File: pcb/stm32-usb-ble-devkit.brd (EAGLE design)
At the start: 90 x 50 mm, 91 parts, among them CN1 USB-MICROB-2TABS, CN2 USB-C-2.0-FEMALE, CN3 USB-C-2.0-FEMALE, Q2 AO3402, Q4 AO3401, Q6 AO3401, Q8 AO3401, U1 STM32F103-48LQFP, U2 STM32F205-64, U3 TUSB320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

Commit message: pcb: Fix symbol orientation and add PSU caps
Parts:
- added C20, C21: 100n, tuetuopay:0805
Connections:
- net +3V3: now also C21.1
- net +5V: now also C20.1
- net GND: now also C20.2, C21.2
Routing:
- net +5V: track 62.0 -> 59.5 mm
- net +3V3: track 245.8 -> 244.8 mm, vias 14 -> 13
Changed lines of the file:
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@@
 <?xml version="1.0" encoding="utf-8"?>
 <!DOCTYPE eagle SYSTEM "eagle.dtd">
-<eagle version="9.0.0">
+<eagle version="9.1.3">
 <drawing>
 <settings>
@@
 <param name="checkStop" value="0"/>
 <param name="checkValues" value="0"/>
+<param name="checkNames" value="1"/>
+<param name="checkWireStubs" value="1"/>
+<param name="checkPolygonWidth" value="0"/>
 <param name="useDiameter" value="13"/>
 <param name="maxErrors" value="50"/>
@@
 <attribute name="VALUE" x="51.265" y="26.238" size="0.0254" layer="27"/>
 </element>
+<element name="C20" library="tuetuopay" package="0805" value="100n" x="-9.9" y="-9.3"/>
+<element name="C21" library="tuetuopay" package="0805" value="100n" x="-9.9" y="-15.45"/>
 </elements>
 <signals>
@@
 <contactref element="C15" pad="2"/>
 <contactref element="C16" pad="2"/>
-<contactref element="C18" pad="1"/>
-<contactref element="U6" pad="2"/>
 <wire x1="12.15" y1="14.75" x2="13.425" y2="13.475" width="0.15" layer="1"/>
 <wire x1="13.425" y1="13.475" x2="14.2432" y2="13.475" width="0.15" layer="1"/>
@@
 <wire x1="16.7" y1="33" x2="13.69644375" y2="33" width="0.15" layer="1"/>
 <wire x1="13.35" y1="32.65355625" x2="13.35" y2="32.4" width="0.15" layer="1"/>
-<wire x1="22.65" y1="37" x2="24.5" y2="37" width="0.4" layer="1"/>
-<wire x1="24.5" y1="37" x2="24.55" y2="37.05" width="0.6" layer="1"/>
-<via x="22.65" y="37" extent="1-16" drill="0.3"/>
 <wire x1="22.65" y1="37" x2="20.7" y2="37" width="0.4" layer="16"/>
 <wire x1="20.7" y1="37" x2="19" y2="35.3" width="0.4" layer="16"/>
 <via x="16.7" y="33" extent="1-16" drill="0.3"/>
 <wire x1="19" y1="35.3" x2="16.7" y2="33" width="0.4" layer="16"/>
-<wire x1="24.55" y1="37.05" x2="25.5" y2="37.05" width="0.4" layer="1"/>
 <wire x1="28.05" y1="39.6" x2="31.05" y2="39.6" width="0.4" layer="1"/>
 <wire x1="31.05" y1="39.6" x2="32.85" y2="39.6" width="0.4" layer="1"/>
@@
 <wire x1="15.73" y1="38.57" x2="19" y2="35.3" width="0.4" layer="16"/>
 <wire x1="5.78649375" y1="38.57" x2="15.73" y2="38.57" width="0.4" layer="16"/>
+<contactref element="C18" pad="1"/>
+<contactref element="U6" pad="2"/>
+<contactref element="C21" pad="1"/>
+<wire x1="22.65" y1="37" x2="24.5" y2="37" width="0.4" layer="1"/>
+<wire x1="24.5" y1="37" x2="24.55" y2="37.05" width="0.6" layer="1"/>
+<wire x1="24.55" y1="37.05" x2="25.5" y2="37.05" width="0" layer="19" extent="1-1"/>
+<wire x1="22.65" y1="37" x2="22.65" y2="37" width="0" layer="19" extent="1-16"/>
+<wire x1="-10.85" y1="-15.45" x2="14.7" y2="9.45" width="0" layer="19" extent="1-1"/>
 </signal>
 <signal name="GND">
@@
 <vertex x="-6.9" y="33.75"/>
 </polygon>
-<wire x1="29.3" y1="22.48" x2="26.85" y2="26.43" width="0" layer="19" extent="1-1"/>
+<contactref element="C20" pad="2"/>
+<contactref element="C21" pad="2"/>
+<wire x1="68.5" y1="38.1" x2="74.65" y2="36.05" width="0" layer="19" extent="1-1"/>
+<wire x1="64.65" y1="34.05" x2="68.5" y2="38.1" width="0" layer="19" extent="1-1"/>
+<wire x1="52.75" y1="33.15" x2="64.65" y2="34.05" width="0" layer="19" extent="1-1"/>
+<wire x1="52.75" y1="29.25" x2="52.75" y2="33.15" width="0" layer="19" extent="1-1"/>
+<wire x1="45.43" y1="33.29" x2="52.75" y2="33.15" width="0" layer="19" extent="1-1"/>
+<wire x1="40.43" y1="35.29" x2="45.43" y2="33.29" width="0" layer="19" extent="1-1"/>
+<wire x1="37.55" y1="33" x2="40.43" y2="35.29" width="0" layer="19" extent="1-1"/>
+<wire x1="37.5375" y1="31.05" x2="37.55" y2="33" width="0" layer="19" extent="1-1"/>
+<wire x1="40.43" y1="39.29" x2="40.43" y2="35.29" width="0" layer="19" extent="1-1"/>
+<wire x1="42.43" y1="41.79" x2="40.43" y2="39.29" width="0" layer="19" extent="1-1"/>
+<wire x1="41.43" y1="45.885" x2="42.43" y2="41.79" width="0" layer="19" extent="1-1"/>
 <wire x1="41.58" y1="48.56" x2="41.43" y2="45.885" width="0" layer="19" extent="1-1"/>
-<wire x1="17.9" y1="17.48" x2="16.05" y2="14.75" width="0" layer="19" extent="1-1"/>
+<wire x1="43.88" y1="48.56" x2="41.58" y2="48.56" width="0" layer="19" extent="1-1"/>
+<wire x1="46.48" y1="48.56" x2="43.88" y2="48.56" width="0" layer="19" extent="1-1"/>
+<wire x1="38.98" y1="48.56" x2="41.58" y2="48.56" width="0" layer="19" extent="1-1"/>
+<wire x1="36.95" y1="42" x2="40.43" y2="39.29" width="0" layer="19" extent="1-1"/>
+<wire x1="34.8375" y1="45.9" x2="36.95" y2="42" width="0" layer="19" extent="1-1"/>
+<wire x1="48.93" y1="39.79" x2="42.43" y2="41.79" width="0" layer="19" extent="1-1"/>
+<wire x1="52.6" y1="40.95" x2="48.93" y2="39.79" width="0" layer="19" extent="1-1"/>
+<wire x1="56.7" y1="43.95" x2="52.6" y2="40.95" width="0" layer="19" extent="1-1"/>
+<wire x1="53.5125" y1="47.85" x2="56.7" y2="43.95" width="0" layer="19" extent="1-1"/>
+<wire x1="31.65" y1="25.9" x2="37.5375" y2="31.05" width="0" layer="19" extent="1-1"/>
+<wire x1="29.3" y1="22.48" x2="31.65" y2="25.9" width="0" layer="19" extent="1-1"/>
+<wire x1="26.85" y1="26.43" x2="29.3" y2="22.48" width="0" layer="19" extent="1-1"/>
+<wire x1="20.35" y1="26.43" x2="26.85" y2="26.43" width="0" layer="19" extent="1-1"/>
+<wire x1="16.7" y1="29.1" x2="20.35" y2="26.43" width="0" layer="19" extent="1-1"/>
 <wire x1="14.15" y1="32.4" x2="16.7" y2="29.1" width="0" layer="19" extent="1-1"/>
-<wire x1="30.85" y1="13.2" x2="26.85" y2="15.03" width="0" layer="19" extent="1-1"/>
-<wire x1="52.6" y1="40.95" x2="56.7" y2="43.95" width="0" layer="19" extent="1-1"/>
+<wire x1="13.75" y1="32.4" x2="14.15" y2="32.4" width="0" layer="19" extent="1-1"/>
+<wire x1="18.4" y1="33" x2="16.7" y2="29.1" width="0" layer="19" extent="1-1"/>
+<wire x1="20.7" y1="36.65" x2="18.4" y2="33" width="0" layer="19" extent="1-1"/>
+<wire x1="22.65" y1="38.9" x2="20.7" y2="36.65" width="0" layer="19" extent="1-1"/>
+<wire x1="24.55" y1="39.35" x2="22.65" y2="38.9" width="0" layer="19" extent="1-1"/>
+<wire x1="9.9375" y1="37.65" x2="13.75" y2="32.4" width="0" layer="19" extent="1-1"/>
+<wire x1="7.355" y1="36.5" x2="9.9375" y2="37.65" width="0" layer="19" extent="1-1"/>
+<wire x1="2.6" y1="21.42" x2="2.6" y2="28.98" width="0" layer="19" extent="1-1"/>
 <wire x1="11.55" y1="10.8375" x2="6.78" y2="12.78" width="0" layer="19" extent="1-1"/>
 <wire x1="15.1" y1="9.45" x2="11.55" y2="10.8375" width="0" layer="19" extent="1-1"/>
+<wire x1="15.5" y1="9.45" x2="15.1" y2="9.45" width="0" layer="19" extent="1-1"/>
+<wire x1="16.05" y1="14.75" x2="15.5" y2="9.45" width="0" layer="19" extent="1-1"/>
+<wire x1="17.9" y1="17.48" x2="16.05" y2="14.75" width="0" layer="19" extent="1-1"/>
+<wire x1="12.15" y1="16.45" x2="16.05" y2="14.75" width="0" layer="19" extent="1-1"/>
+<wire x1="26.85" y1="15.03" x2="29.3" y2="22.48" width="0" layer="19" extent="1-1"/>
+<wire x1="30.85" y1="13.2" x2="26.85" y2="15.03" width="0" layer="19" extent="1-1"/>
+<wire x1="25.05" y1="9.9375" x2="26.85" y2="15.03" width="0" layer="19" extent="1-1"/>
+<wire x1="36.45" y1="6.95" x2="30.85" y2="13.2" width="0" layer="19" extent="1-1"/>
+<wire x1="43.6" y1="24" x2="37.5375" y2="31.05" width="0" layer="19" extent="1-1"/>
+<wire x1="45.05" y1="24" x2="43.6" y2="24" width="0" layer="19" extent="1-1"/>
+<wire x1="39.45" y1="19.85" x2="43.6" y2="24" width="0" layer="19" extent="1-1"/>
+<wire x1="39.45" y1="18.4" x2="39.45" y2="19.85" width="0" layer="19" extent="1-1"/>
+<wire x1="-8.95" y1="-9.3" x2="2.6" y2="12.78" width="0" layer="19" extent="1-1"/>
+<wire x1="-8.95" y1="-15.45" x2="-8.95" y2="-9.3" width="0" layer="19" extent="1-1"/>
 </signal>
 <signal name="STLINK_PC13">
@@
 <contactref element="Q6" pad="2"/>
 <contactref element="Q8" pad="2"/>
-<contactref element="C19" pad="1"/>
-<contactref element="U6" pad="3"/>
 <contactref element="D1" pad="3"/>
 <contactref element="Q4" pad="3"/>
@@
 <wire x1="15.45" y1="43.5556625" x2="15.45" y2="39" width="0.4" layer="1"/>
 <wire x1="15.45" y1="39" x2="14.9" y2="38.45" width="0.4" layer="1"/>
-<wire x1="20.7" y1="34.75" x2="24.55" y2="34.75" width="0.4" layer="1"/>
 <via x="14.9" y="36.65" extent="1-16" drill="0.3"/>
 <wire x1="14.9" y1="36.65" x2="16.3" y2="36.65" width="0.4" layer="16"/>
@@
 <via x="17.55" y="35.4" extent="1-16" drill="0.3"/>
 <wire x1="17.55" y1="35.4" x2="18.2" y2="34.75" width="0.4" layer="1"/>
-<wire x1="18.2" y1="34.75" x2="20.7" y2="34.75" width="0.4" layer="1"/>
 <via x="16.4" y="12.95" extent="1-16" drill="0.4"/>
 <wire x1="16.4" y1="12.95" x2="15.25" y2="14.1" width="0.4" layer="16"/>
@@
 <wire x1="20.675" y1="17.668625" x2="20.675" y2="24.325" width="0.4" layer="16"/>
 <wire x1="15.9" y1="29.1" x2="15.9" y2="33.75" width="0.4" layer="16"/>
+<contactref element="C19" pad="1"/>
+<contactref element="U6" pad="3"/>
+<contactref element="C20" pad="1"/>
+<wire x1="20.7" y1="34.75" x2="24.55" y2="34.75" width="0.4" layer="1"/>
+<wire x1="18.2" y1="34.75" x2="20.7" y2="34.75" width="0" layer="19" extent="1-1"/>
+<wire x1="-10.85" y1="-9.3" x2="15.25" y2="14.1" width="0" layer="19" extent="1-16"/>
 </signal>
 <signal name="STM_DBG_PIN2">
@@
 </signal>
 </signals>
+<mfgpreviewcolors>
+<mfgpreviewcolor name="soldermaskcolor" color="0xC8008000"/>
+<mfgpreviewcolor name="silkscreencolor" color="0xFFFEFEFE"/>
+<mfgpreviewcolor name="backgroundcolor" color="0xFF282828"/>
+<mfgpreviewcolor name="coppercolor" color="0xFFFFBF00"/>
+<mfgpreviewcolor name="substratecolor" color="0xFF786E46"/>
+</mfgpreviewcolors>
 <errors>
 </errors>

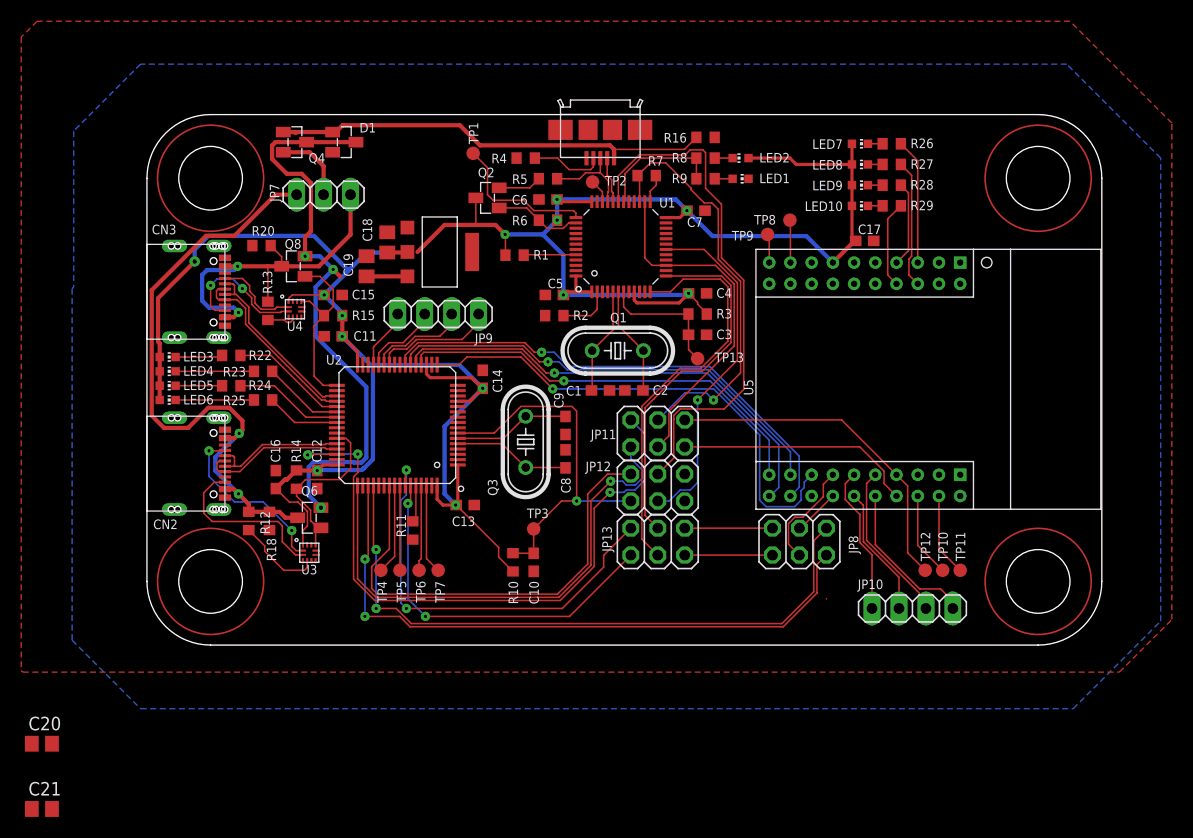
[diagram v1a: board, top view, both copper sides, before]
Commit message: pcb: Done groundplane
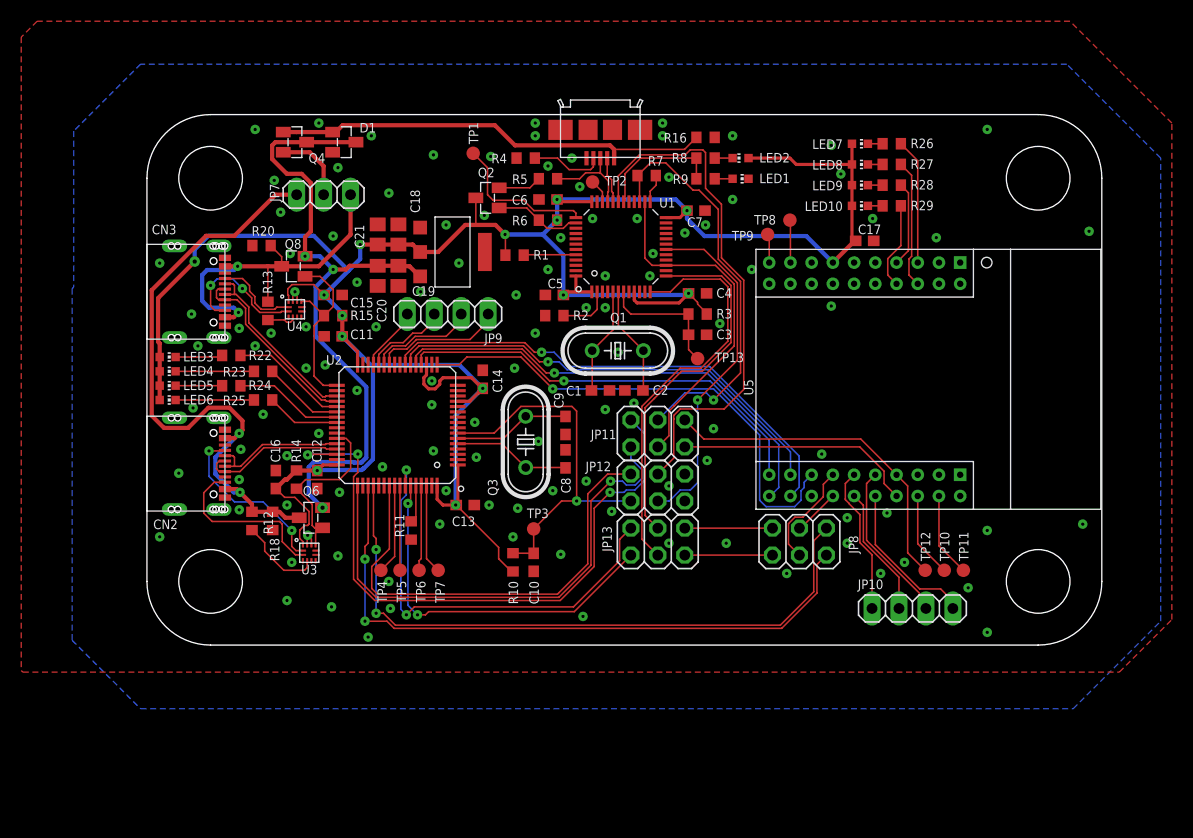
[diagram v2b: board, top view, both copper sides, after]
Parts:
- moved C21 62.7 mm to (21.8, 38.7), turned to 90 degrees
- moved C20 54.3 mm to (21.8, 34.8), turned to 270 degrees
- moved C19 3.13 mm to (23.7, 34.8), turned to 270 degrees
- moved C18 1.29 mm to (23.7, 38.7)
- moved U6 1.20 mm to (28.8, 37.0)
- moved JP9 0.90 mm to (28.4, 31.2)
- moved R12 0.30 mm to (9.90, 11.7)
- moved R18 0.30 mm to (11.8, 11.7)
- moved TP11 0.30 mm to (77.0, 7.05)
- moved TP10 0.15 mm to (75.2, 7.05)
- moved R11 0.15 mm to (24.9, 10.8)
- moved Q6 0.15 mm to (15.4, 12.0)
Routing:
- net +3V3: track 244.8 -> 250.9 mm, vias 13 -> 14
- net +5V: track 59.5 -> 63.5 mm
- net GND: track 0.00 -> 3.93 mm, vias 0 -> 116
- net STM_TX: track 39.9 -> 41.3 mm
- net STM_DBG_PIN0: track 11.5 -> 12.3 mm
- net STM_DBG_PIN2: track 7.35 -> 8.13 mm
- net STM_DBG_PIN1: track 9.50 -> 10.2 mm

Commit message: pcb: Add SPI PU/PD resistors
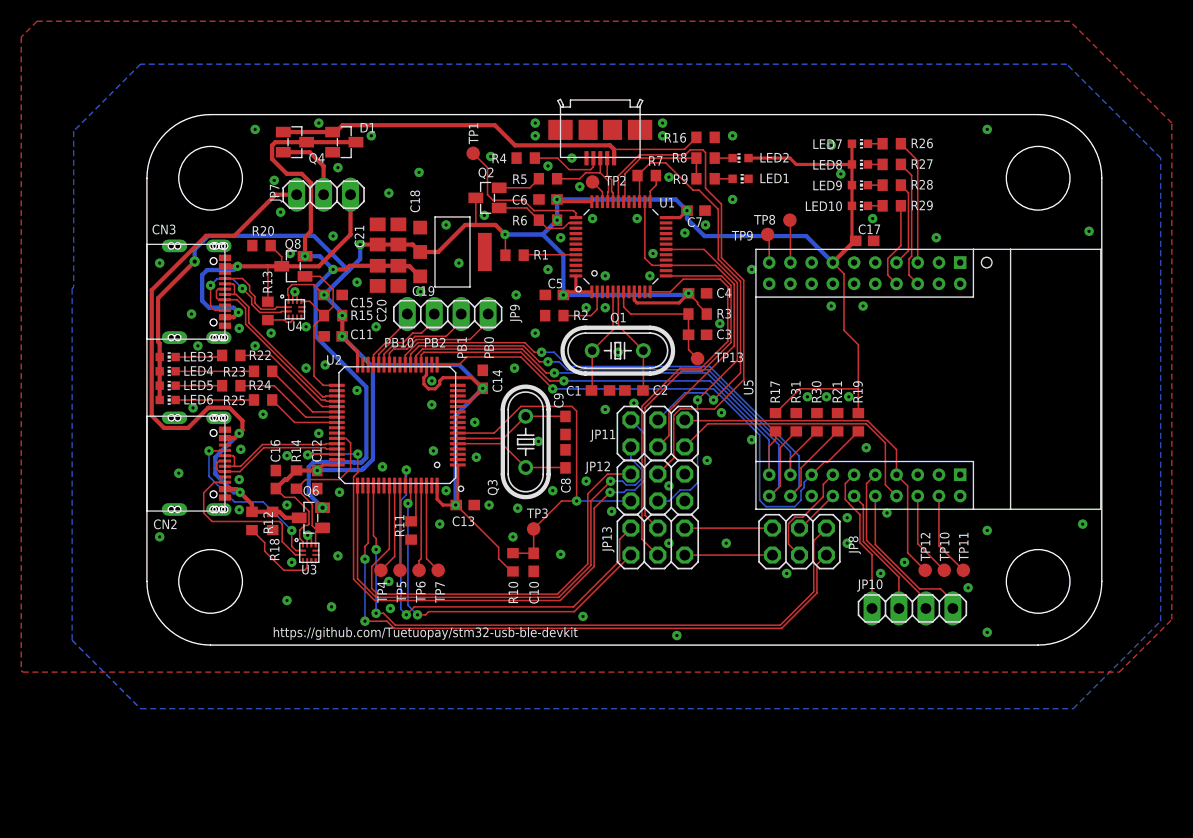
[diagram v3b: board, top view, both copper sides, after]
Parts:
- added R17, R19, R21, R30, R31: 100k, tuetuopay:R0603
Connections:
- net +3V3: now also R17.2, R19.2
- net GND: now also R21.1, R30.1, R31.1
- net SPI_CS: now also R19.1
- net SPI_IRQ: now also R17.1
- net SPI_MISO: now also R30.2
- net SPI_MOSI: now also R21.2
- net SPI_SCK: now also R31.2
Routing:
- net +3V3: track 250.9 -> 274.8 mm
- net SPI_MOSI: track 47.0 -> 55.0 mm
- net SPI_SCK: track 44.3 -> 51.5 mm
- net SPI_CS: track 47.1 -> 53.2 mm
- net SPI_MISO: track 43.4 -> 48.5 mm
- net SPI_IRQ: track 40.5 -> 44.9 mm
- net NRF_SWCLK: track 22.6 -> 26.0 mm
- net NRF_SWDIO: track 32.2 -> 33.7 mm
- net SWO: track 49.3 -> 48.8 mm
- net GND: vias 116 -> 121
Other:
- board text added: "PB0"
- board text added: "PB1"
- board text added: "PB10"
- board text added: "PB2"
- board text added: "https://github.com/Tuetuopay/stm32-usb-ble-devkit"
